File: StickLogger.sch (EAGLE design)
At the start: 51 parts, among them IC1 4050D, U1 ATMEGA328P-MU, U4 DS1307, X1 MICROSD, Y1 16MHZ, Y2 32.768kHz

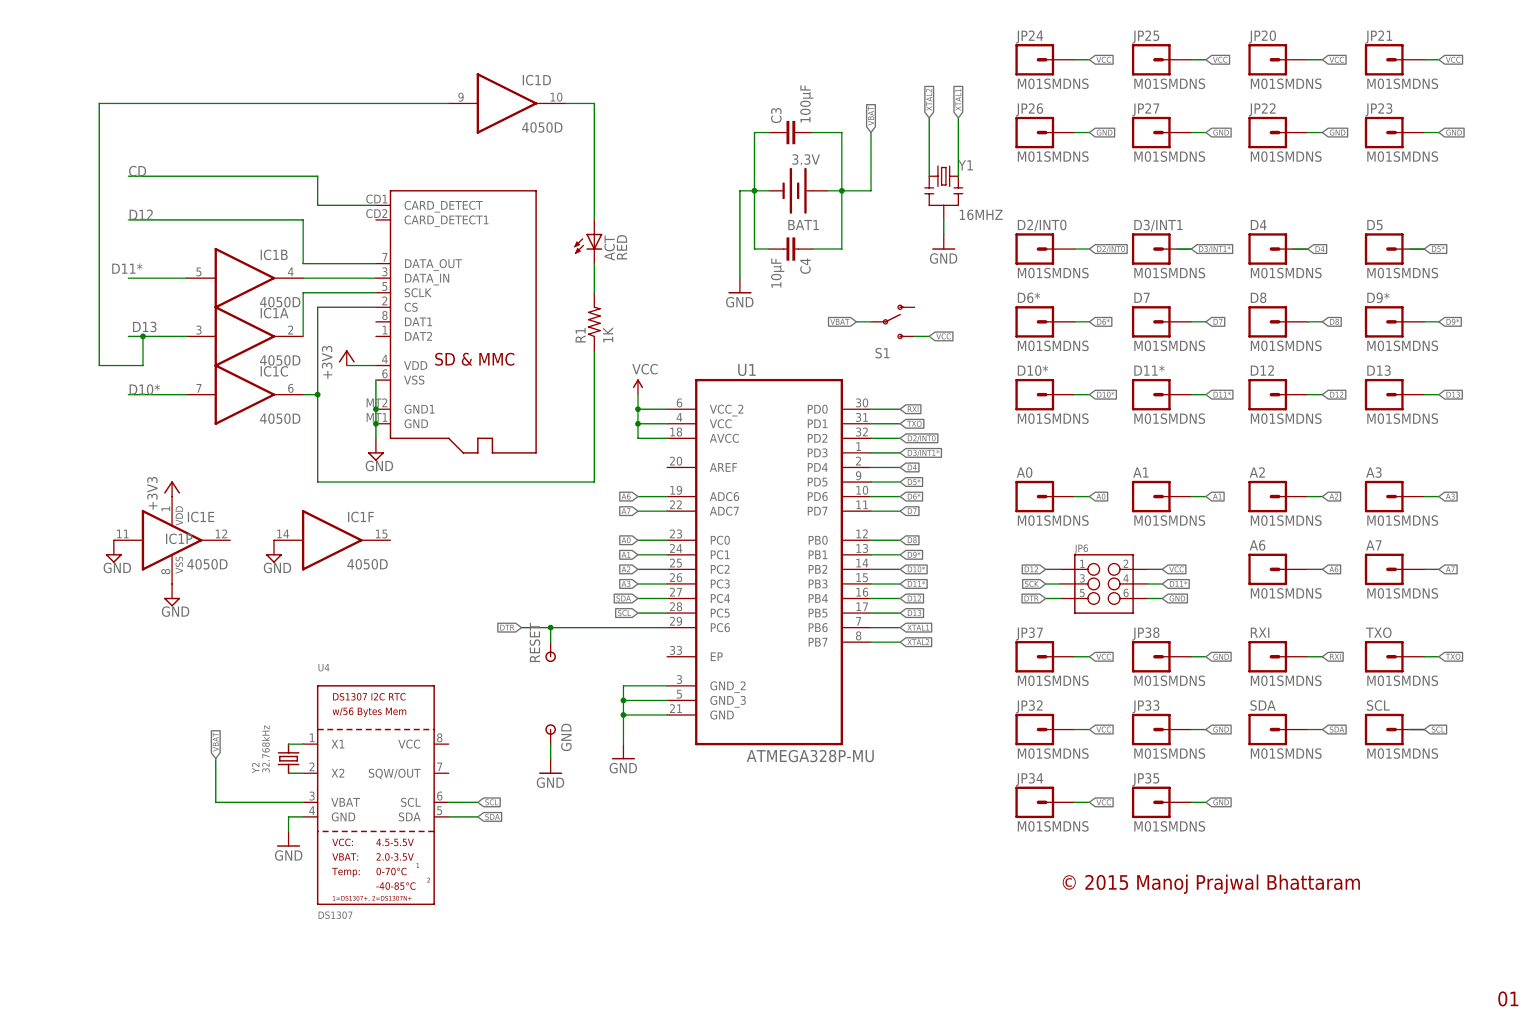
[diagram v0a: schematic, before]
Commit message: Renamed project to StickLogger
New board design
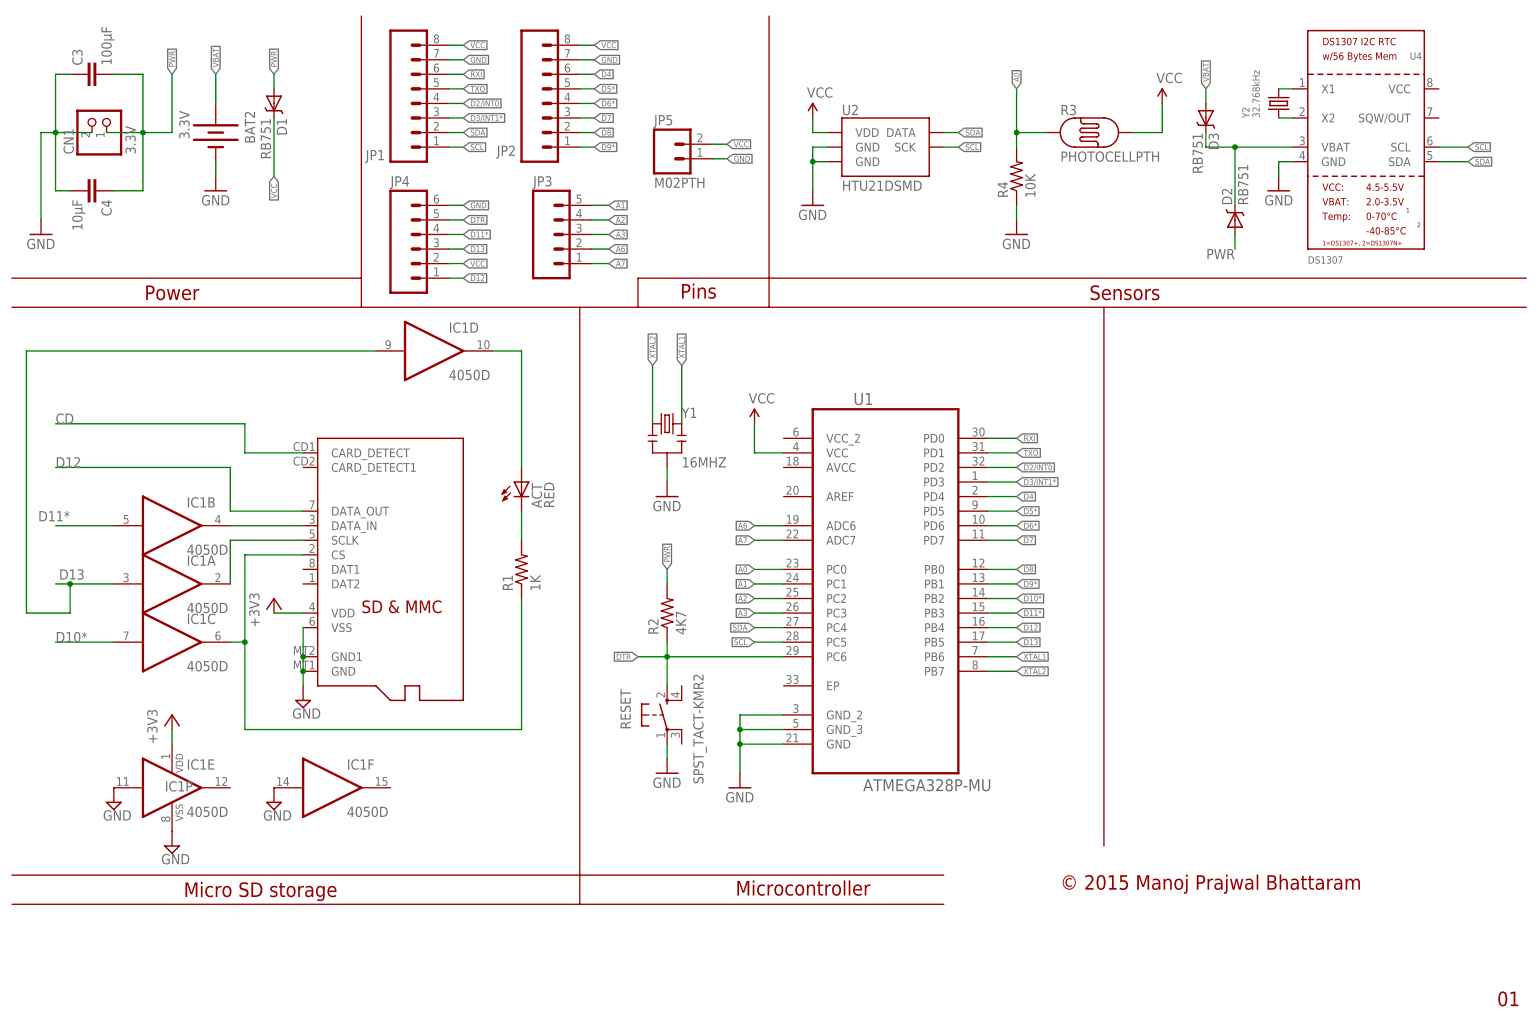
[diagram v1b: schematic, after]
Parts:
- removed A0, A1, A2, A3, A6, A7, D10*, D11*, D12, D13, D2/INT0, D3/INT1, D4, D5, D6*, D7, D8, D9*, JP20, JP21, JP22, JP23, JP24, JP25, JP26, JP27, JP32, JP33, JP34, JP35, JP37, JP38, RXI, SCL, SDA, TXO: M01SMDNS, SparkFun-Connectors:M01SMDNS
- removed BAT1: 3.3V, SparkFun-Electromechanical:BATTERY20SMD
- removed GND: PAD-TESTPOINT, ee2parts:PAD-TESTPOINT
- removed JP6: (no value), SparkFun-Connectors:M03X2POGO_PINS
- removed S1: (no value), SparkFun-Electromechanical:SWITCH-SPDT-SMD-A
- added BAT2: 3.3V, SparkFun-Electromechanical:BATTERY12MM
- added CN1: 3.3V, adafruit:JST_2PIN-SMT-RA
- added D1, D2, D3: RB751, SparkFun-DiscreteSemi:DIODE-SCHOTTKY-RB751
- added JP1, JP2: (no value), SparkFun-Connectors:M08NO_SILK
- added JP3: (no value), SparkFun-Connectors:M05NO_SILK
- added JP4: (no value), SparkFun-Connectors:M06SMD
- added JP5: M02PTH, SparkFun-Connectors:M02PTH
- added R2: 4K7, SparkFun-Passives:RESISTOR0402-RES
- added R3: PHOTOCELLPTH, SparkFun-Sensors:PHOTOCELLPTH
- added R4: 10K, SparkFun-Passives:RESISTOR0402-RES
- added U2: HTU21DSMD, SparkFun-Sensors:HTU21DSMD
- RESET: value PAD-TESTPOINT -> SPST_TACT-KMR2; device ee2parts:PAD-TESTPOINT -> adafruit:SPST_TACT-KMR2
- Y2: device microbuilder:CRYSTAL8X3.8SMT -> SparkFun-FreqCtrl:CRYSTAL32-SMD
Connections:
- removed net SCK: JP6.3
- new net 3V: D2.C, D3.C, U4.VBAT
- new net PWR: C3.2, C4.1, CN1.2, D1.A, D2.A, R2.2
- net A0: now also R3.P$1, R4.2; no longer A0.1
- net A1: now also JP3.5; no longer A1.1
- net A2: now also JP3.4; no longer A2.1
- net A3: now also JP3.3; no longer A3.1
- net A6: now also JP3.2; no longer A6.1
- net A7: now also JP3.1; no longer A7.1
- net D10*: no longer D10*.1
- net D11*: now also JP4.4; no longer D11*.1, JP6.4
- net D12: now also JP4.1; no longer D12.1, JP6.1
- net D13: now also JP4.3; no longer D13.1
- net D2/INT0: now also JP1.4; no longer D2/INT0.1
- net D3/INT1*: now also JP1.3; no longer D3/INT1.1
- net D4: now also JP2.6; no longer D4.1
- net D5*: now also JP2.5; no longer D5.1
- net D6*: now also JP2.4; no longer D6*.1
- net D7: now also JP2.3; no longer D7.1
- net D8: now also JP2.2; no longer D8.1
- net D9*: now also JP2.1; no longer D9*.1
- net DTR: now also JP4.5, R2.1, RESET.S; no longer JP6.5, RESET.P
- net GND: now also BAT2.-, CN1.1, JP1.7, JP2.7, JP4.6, JP5.1, R4.1, RESET.P, U2.GND@2, U2.GND@7; no longer BAT1.-, GND.P, JP22.1, JP23.1, JP26.1, JP27.1, JP33.1, JP35.1, JP38.1, JP6.6
- net RXI: now also JP1.6; no longer RXI.1
- net SCL: now also JP1.1, U2.SCK; no longer SCL.1
- net SDA: now also JP1.2, U2.DATA; no longer SDA.1
- net TXO: now also JP1.5; no longer TXO.1
- net VBAT: now also BAT2.+, D3.A; no longer BAT1.+, C3.2, C4.1, S1.P, U4.VBAT
- net VCC: now also D1.C, JP1.8, JP2.8, JP4.2, JP5.2, R3.P$2, U2.VDD; no longer JP20.1, JP21.1, JP24.1, JP25.1, JP32.1, JP34.1, JP37.1, JP6.2, S1.S, U1.AVCC, U1.VCC_2
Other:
- note added: "Micro SD storage"
- note added: "Microcontroller"
- note added: "Pins"
- note added: "Power"
- note added: "Sensors"
- moved on the sheet: ACT, C3, C4, IC1A, IC1B, IC1C, IC1D, IC1E, IC1F, IC1P, R1, U1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
